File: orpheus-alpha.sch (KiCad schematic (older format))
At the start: 56 parts, among them J1 Signal in, J2 AC in, J3 Signal out, J4 uC, U1 OPA2134, U2 PGA2311, U3 LM317_3PinPackage, U4 LM337_SOT223, U5 LM7805_TO220

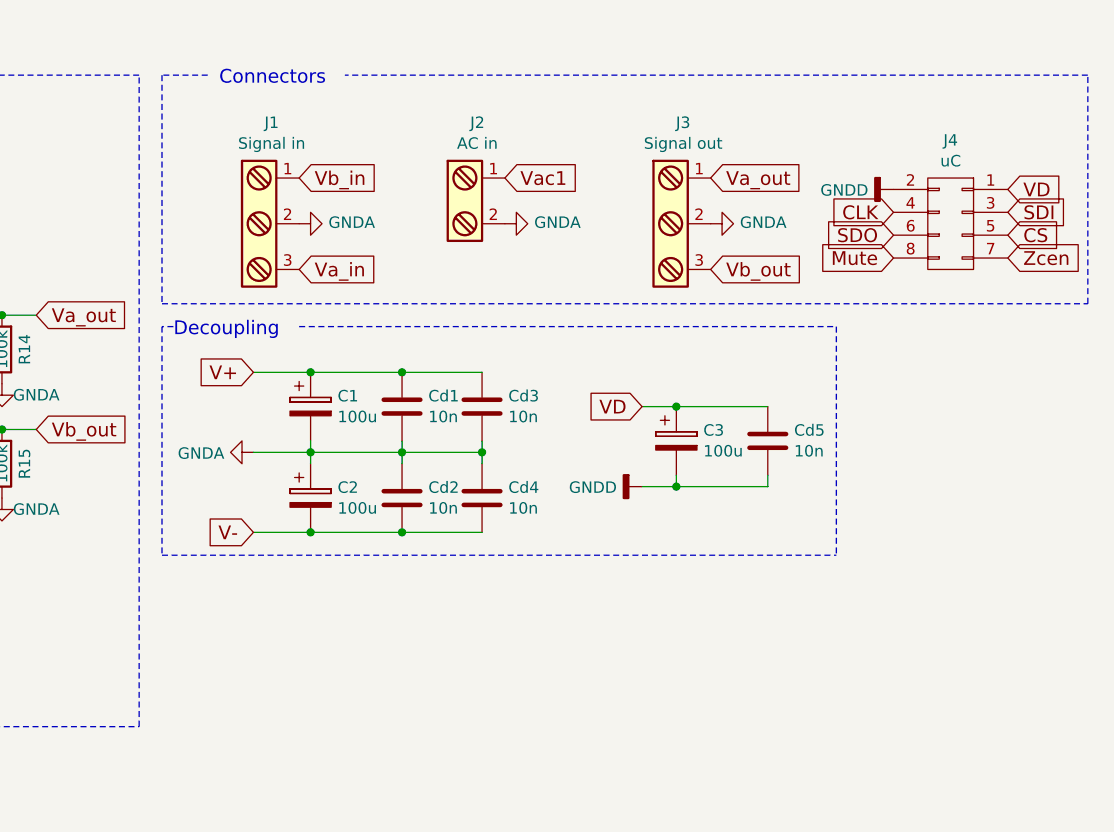
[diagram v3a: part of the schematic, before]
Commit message: Added optional power connectors
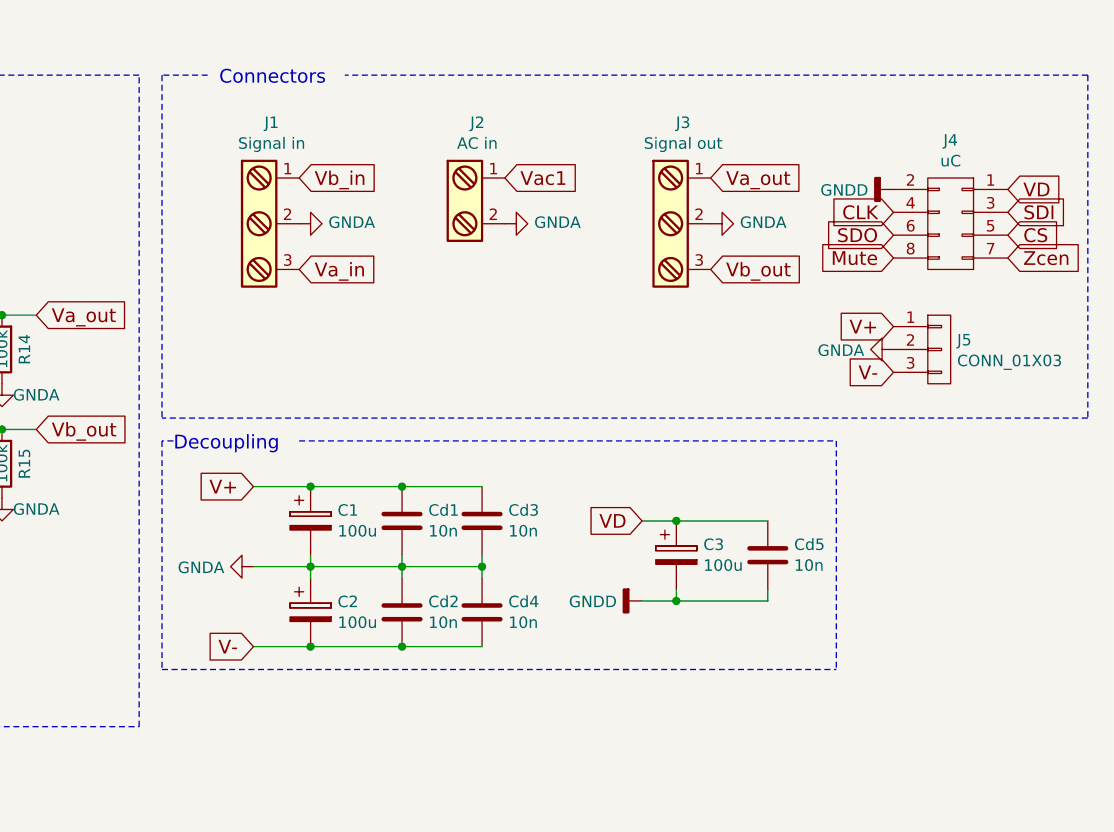
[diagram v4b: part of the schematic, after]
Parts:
- added J5: CONN_01X03, Pin_Headers:Pin_Header_Straight_1x03_Pitch2.54mm, symbol CONN_01X03
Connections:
- net GNDA: now also J5.2 (P2)
- net V+: now also J5.1 (P1)
- net V-: now also J5.3 (P3)
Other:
- moved on the sheet: C1, C2, C3, Cd1, Cd2, Cd3, Cd4, Cd5
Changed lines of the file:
@@
 Text GLabel 2150 1400 3    60   Input ~ 0
 V-
-Text GLabel 7050 1850 0    60   Input ~ 0
+Text GLabel 7050 2350 0    60   Input ~ 0
 V+
-Text GLabel 7050 2550 0    60   Input ~ 0
+Text GLabel 7050 3050 0    60   Input ~ 0
 V-
 $Comp
 L C Cd1
 U 1 1 59B85869
-P 7700 2000
-F 0 "Cd1" H 7815 2046 50  0000 L CNN
-F 1 "10n" H 7815 1955 50  0000 L CNN
-F 2 "Capacitors_SMD:C_0603_HandSoldering" H 7738 1850 50  0001 C CNN
-F 3 "" H 7700 2000 50  0001 C CNN
-F 4 "06035C103JAT2A" H 7700 2000 60  0001 C CNN "manf#"
-	1    7700 2000
+P 7700 2500
+F 0 "Cd1" H 7815 2546 50  0000 L CNN
+F 1 "10n" H 7815 2455 50  0000 L CNN
+F 2 "Capacitors_SMD:C_0603_HandSoldering" H 7738 2350 50  0001 C CNN
+F 3 "" H 7700 2500 50  0001 C CNN
+F 4 "06035C103JAT2A" H 7700 2500 60  0001 C CNN "manf#"
+	1    7700 2500
 	1    0    0    -1
 $EndComp
@@
 L C Cd2
 U 1 1 59B858A9
-P 7700 2400
-F 0 "Cd2" H 7815 2446 50  0000 L CNN
-F 1 "10n" H 7815 2355 50  0000 L CNN
-F 2 "Capacitors_SMD:C_0603_HandSoldering" H 7738 2250 50  0001 C CNN
-F 3 "" H 7700 2400 50  0001 C CNN
-F 4 "06035C103JAT2A" H 7700 2400 60  0001 C CNN "manf#"
-	1    7700 2400
+P 7700 2900
+F 0 "Cd2" H 7815 2946 50  0000 L CNN
+F 1 "10n" H 7815 2855 50  0000 L CNN
+F 2 "Capacitors_SMD:C_0603_HandSoldering" H 7738 2750 50  0001 C CNN
+F 3 "" H 7700 2900 50  0001 C CNN
+F 4 "06035C103JAT2A" H 7700 2900 60  0001 C CNN "manf#"
+	1    7700 2900
 	1    0    0    -1
 $EndComp
@@
 L CP C1
 U 1 1 59B85A85
-P 7300 2000
-F 0 "C1" H 7418 2046 50  0000 L CNN
-F 1 "100u" H 7418 1955 50  0000 L CNN
-F 2 "Capacitors_THT:CP_Radial_D5.0mm_P2.00mm" H 7338 1850 50  0001 C CNN
-F 3 "" H 7300 2000 50  0001 C CNN
-F 4 "UFW1C101MDD1TD" H 7300 2000 60  0001 C CNN "manf#"
-F 5 "16V" H 7300 2000 60  0001 C CNN "Voltage"
-	1    7300 2000
+P 7300 2500
+F 0 "C1" H 7418 2546 50  0000 L CNN
+F 1 "100u" H 7418 2455 50  0000 L CNN
+F 2 "Capacitors_THT:CP_Radial_D5.0mm_P2.00mm" H 7338 2350 50  0001 C CNN
+F 3 "" H 7300 2500 50  0001 C CNN
+F 4 "UFW1C101MDD1TD" H 7300 2500 60  0001 C CNN "manf#"
+F 5 "16V" H 7300 2500 60  0001 C CNN "Voltage"
+	1    7300 2500
 	1    0    0    -1
 $EndComp
@@
 L CP C2
 U 1 1 59B85AD5
-P 7300 2400
-F 0 "C2" H 7418 2446 50  0000 L CNN
-F 1 "100u" H 7418 2355 50  0000 L CNN
-F 2 "Capacitors_THT:CP_Radial_D5.0mm_P2.00mm" H 7338 2250 50  0001 C CNN
-F 3 "" H 7300 2400 50  0001 C CNN
-F 4 "16V" H 7300 2400 60  0001 C CNN "Voltage"
-	1    7300 2400
+P 7300 2900
+F 0 "C2" H 7418 2946 50  0000 L CNN
+F 1 "100u" H 7418 2855 50  0000 L CNN
+F 2 "Capacitors_THT:CP_Radial_D5.0mm_P2.00mm" H 7338 2750 50  0001 C CNN
+F 3 "" H 7300 2900 50  0001 C CNN
+F 4 "16V" H 7300 2900 60  0001 C CNN "Voltage"
+	1    7300 2900
 	1    0    0    -1
 $EndComp
@@
 L C Cd3
 U 1 1 59B85DFC
-P 8050 2000
-F 0 "Cd3" H 8165 2046 50  0000 L CNN
-F 1 "10n" H 8165 1955 50  0000 L CNN
-F 2 "Capacitors_SMD:C_0603_HandSoldering" H 8088 1850 50  0001 C CNN
-F 3 "" H 8050 2000 50  0001 C CNN
-F 4 "06035C103JAT2A" H 8050 2000 60  0001 C CNN "manf#"
-	1    8050 2000
+P 8050 2500
+F 0 "Cd3" H 8165 2546 50  0000 L CNN
+F 1 "10n" H 8165 2455 50  0000 L CNN
+F 2 "Capacitors_SMD:C_0603_HandSoldering" H 8088 2350 50  0001 C CNN
+F 3 "" H 8050 2500 50  0001 C CNN
+F 4 "06035C103JAT2A" H 8050 2500 60  0001 C CNN "manf#"
+	1    8050 2500
 	1    0    0    -1
 $EndComp
@@
 L C Cd4
 U 1 1 59B85E65
-P 8050 2400
-F 0 "Cd4" H 8165 2446 50  0000 L CNN
-F 1 "10n" H 8165 2355 50  0000 L CNN
-F 2 "Capacitors_SMD:C_0603_HandSoldering" H 8088 2250 50  0001 C CNN
-F 3 "" H 8050 2400 50  0001 C CNN
-F 4 "06035C103JAT2A" H 8050 2400 60  0001 C CNN "manf#"
-	1    8050 2400
-	1    0    0    -1
-$EndComp
-Text Notes 6700 1700 0    60   ~ 0
+P 8050 2900
+F 0 "Cd4" H 8165 2946 50  0000 L CNN
+F 1 "10n" H 8165 2855 50  0000 L CNN
+F 2 "Capacitors_SMD:C_0603_HandSoldering" H 8088 2750 50  0001 C CNN
+F 3 "" H 8050 2900 50  0001 C CNN
+F 4 "06035C103JAT2A" H 8050 2900 60  0001 C CNN "manf#"
+	1    8050 2900
+	1    0    0    -1
+$EndComp
+Text Notes 6700 2200 0    60   ~ 0
 Decoupling
 $Comp
@@
 Text Notes 6900 600  0    60   ~ 0
 Connectors
-Text GLabel 8750 2000 0    60   Input ~ 0
+Text GLabel 8750 2500 0    60   Input ~ 0
 VD
 $Comp
 L CP C3
 U 1 1 59B8A02A
-P 8900 2150
-F 0 "C3" H 9018 2196 50  0000 L CNN
-F 1 "100u" H 9018 2105 50  0000 L CNN
-F 2 "Capacitors_THT:CP_Radial_D5.0mm_P2.00mm" H 8938 2000 50  0001 C CNN
-F 3 "" H 8900 2150 50  0001 C CNN
-F 4 "16V" H 8900 2150 60  0001 C CNN "Voltage"
-	1    8900 2150
+P 8900 2650
+F 0 "C3" H 9018 2696 50  0000 L CNN
+F 1 "100u" H 9018 2605 50  0000 L CNN
+F 2 "Capacitors_THT:CP_Radial_D5.0mm_P2.00mm" H 8938 2500 50  0001 C CNN
+F 3 "" H 8900 2650 50  0001 C CNN
+F 4 "16V" H 8900 2650 60  0001 C CNN "Voltage"
+	1    8900 2650
 	1    0    0    -1
 $EndComp
@@
 L C Cd5
 U 1 1 59B8A06F
-P 9300 2150
-F 0 "Cd5" H 9415 2196 50  0000 L CNN
-F 1 "10n" H 9415 2105 50  0000 L CNN
-F 2 "Capacitors_SMD:C_0603_HandSoldering" H 9338 2000 50  0001 C CNN
-F 3 "" H 9300 2150 50  0001 C CNN
-F 4 "06035C103JAT2A" H 9300 2150 60  0001 C CNN "manf#"
-	1    9300 2150
+P 9300 2650
+F 0 "Cd5" H 9415 2696 50  0000 L CNN
+F 1 "10n" H 9415 2605 50  0000 L CNN
+F 2 "Capacitors_SMD:C_0603_HandSoldering" H 9338 2500 50  0001 C CNN
+F 3 "" H 9300 2650 50  0001 C CNN
+F 4 "06035C103JAT2A" H 9300 2650 60  0001 C CNN "manf#"
+	1    9300 2650
 	1    0    0    -1
 $EndComp
@@
 Connection ~ 1100 1000
 Wire Wire Line
-	7050 1850 8050 1850
-Wire Wire Line
-	7050 2550 8050 2550
-Wire Wire Line
-	7050 2200 8050 2200
-Connection ~ 7300 1850
-Wire Wire Line
-	7300 2150 7300 2250
-Connection ~ 7300 2200
-Wire Wire Line
-	8050 2150 8050 2250
-Connection ~ 8050 2200
-Connection ~ 7700 1850
-Wire Wire Line
-	7700 2150 7700 2250
-Connection ~ 7700 2200
-Connection ~ 7300 2550
-Connection ~ 7700 2550
-Wire Notes Line
-	6700 1650 6650 1650
-Wire Notes Line
-	6650 1650 6650 2650
-Wire Notes Line
-	6650 2650 9600 2650
-Wire Notes Line
-	7250 1650 9600 1650
+	7050 2350 8050 2350
+Wire Wire Line
+	7050 3050 8050 3050
+Wire Wire Line
+	7050 2700 8050 2700
+Connection ~ 7300 2350
+Wire Wire Line
+	7300 2650 7300 2750
+Connection ~ 7300 2700
+Wire Wire Line
+	8050 2650 8050 2750
+Connection ~ 8050 2700
+Connection ~ 7700 2350
+Wire Wire Line
+	7700 2650 7700 2750
+Connection ~ 7700 2700
+Connection ~ 7300 3050
+Connection ~ 7700 3050
+Wire Notes Line
+	6700 2150 6650 2150
+Wire Notes Line
+	6650 2150 6650 3150
+Wire Notes Line
+	6650 3150 9600 3150
+Wire Notes Line
+	7250 2150 9600 2150
 Wire Wire Line
 	1500 3750 2000 3750
@@
 	6850 550  6650 550
 Wire Notes Line
-	6650 550  6650 1550
-Wire Notes Line
-	6650 1550 10700 1550
-Wire Notes Line
-	10700 1550 10700 550
+	6650 550  6650 2050
+Wire Notes Line
+	10700 550  10700 2050
 Wire Notes Line
 	10700 550  7450 550
 Wire Wire Line
-	8750 2000 9300 2000
-Wire Wire Line
-	9300 2350 9300 2300
-Wire Wire Line
-	8750 2350 9300 2350
-Wire Wire Line
-	8900 2300 8900 2350
-Connection ~ 8900 2350
-Connection ~ 8900 2000
-Wire Notes Line
-	9600 1650 9600 2650
+	8750 2500 9300 2500
+Wire Wire Line
+	9300 2850 9300 2800
+Wire Wire Line
+	8750 2850 9300 2850
+Wire Wire Line
+	8900 2800 8900 2850
+Connection ~ 8900 2850
+Connection ~ 8900 2500
+Wire Notes Line
+	9600 2150 9600 3150
 Wire Wire Line
 	900  6350 900  5850
@@
 L GNDA #PWR09
 U 1 1 59BC7B64
-P 7050 2200
-F 0 "#PWR09" H 7050 1950 50  0001 C CNN
-F 1 "GNDA" V 7055 2073 50  0000 R CNN
-F 2 "" H 7050 2200 50  0001 C CNN
-F 3 "" H 7050 2200 50  0001 C CNN
-	1    7050 2200
+P 7050 2700
+F 0 "#PWR09" H 7050 2450 50  0001 C CNN
+F 1 "GNDA" V 7055 2573 50  0000 R CNN
+F 2 "" H 7050 2700 50  0001 C CNN
+F 3 "" H 7050 2700 50  0001 C CNN
+	1    7050 2700
 	0    1    1    0
 $EndComp
@@
 L GNDD #PWR011
 U 1 1 59BC7D4A
-P 8750 2350
-F 0 "#PWR011" H 8750 2100 50  0001 C CNN
-F 1 "GNDD" V 8754 2240 50  0000 R CNN
-F 2 "" H 8750 2350 50  0001 C CNN
-F 3 "" H 8750 2350 50  0001 C CNN
-	1    8750 2350
+P 8750 2850
+F 0 "#PWR011" H 8750 2600 50  0001 C CNN
+F 1 "GNDD" V 8754 2740 50  0000 R CNN
+F 2 "" H 8750 2850 50  0001 C CNN
+F 3 "" H 8750 2850 50  0001 C CNN
+	1    8750 2850
 	0    1    1    0
 $EndComp
@@
 	8650 5250 8650 5700
 Connection ~ 8650 5700
+$Comp
+L CONN_01X03 J5
+U 1 1 59E385EB
+P 10050 1750
+F 0 "J5" H 10128 1791 50  0000 L CNN
+F 1 "CONN_01X03" H 10128 1700 50  0000 L CNN
+F 2 "Pin_Headers:Pin_Header_Straight_1x03_Pitch2.54mm" H 10050 1750 50  0001 C CNN
+F 3 "" H 10050 1750 50  0001 C CNN
+	1    10050 1750
+	1    0    0    -1
+$EndComp
+$Comp
+L GNDA #PWR019
+U 1 1 59E38737
+P 9850 1750
+F 0 "#PWR019" H 9850 1500 50  0001 C CNN
+F 1 "GNDA" V 9855 1622 50  0000 R CNN
+F 2 "" H 9850 1750 50  0001 C CNN
+F 3 "" H 9850 1750 50  0001 C CNN
+	1    9850 1750
+	0    1    1    0
+$EndComp
+Text GLabel 9850 1650 0    60   Input ~ 0
+V+
+Text GLabel 9850 1850 0    60   Input ~ 0
+V-
+Wire Notes Line
+	10700 2050 6650 2050
 $EndSCHEMATC

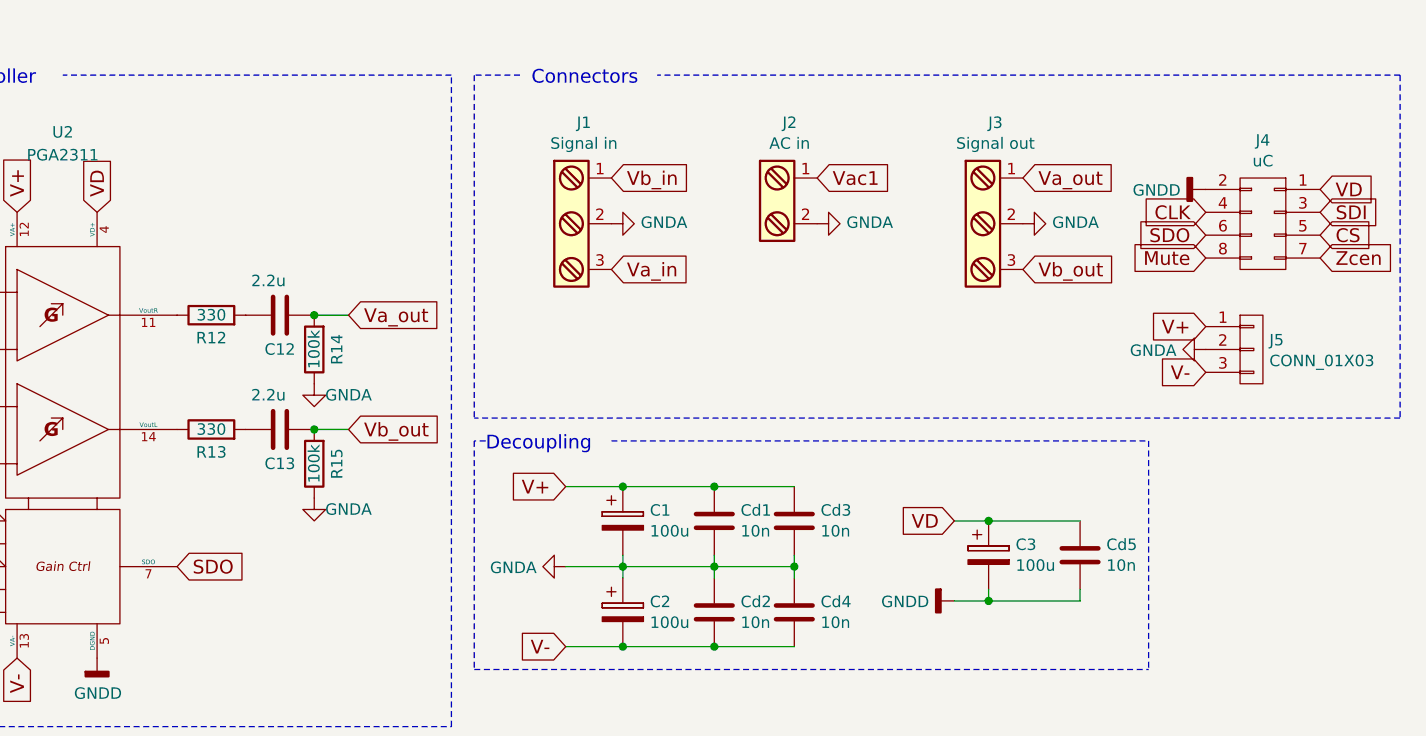
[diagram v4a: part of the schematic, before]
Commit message: New layout, "debug" connection pads at the edge
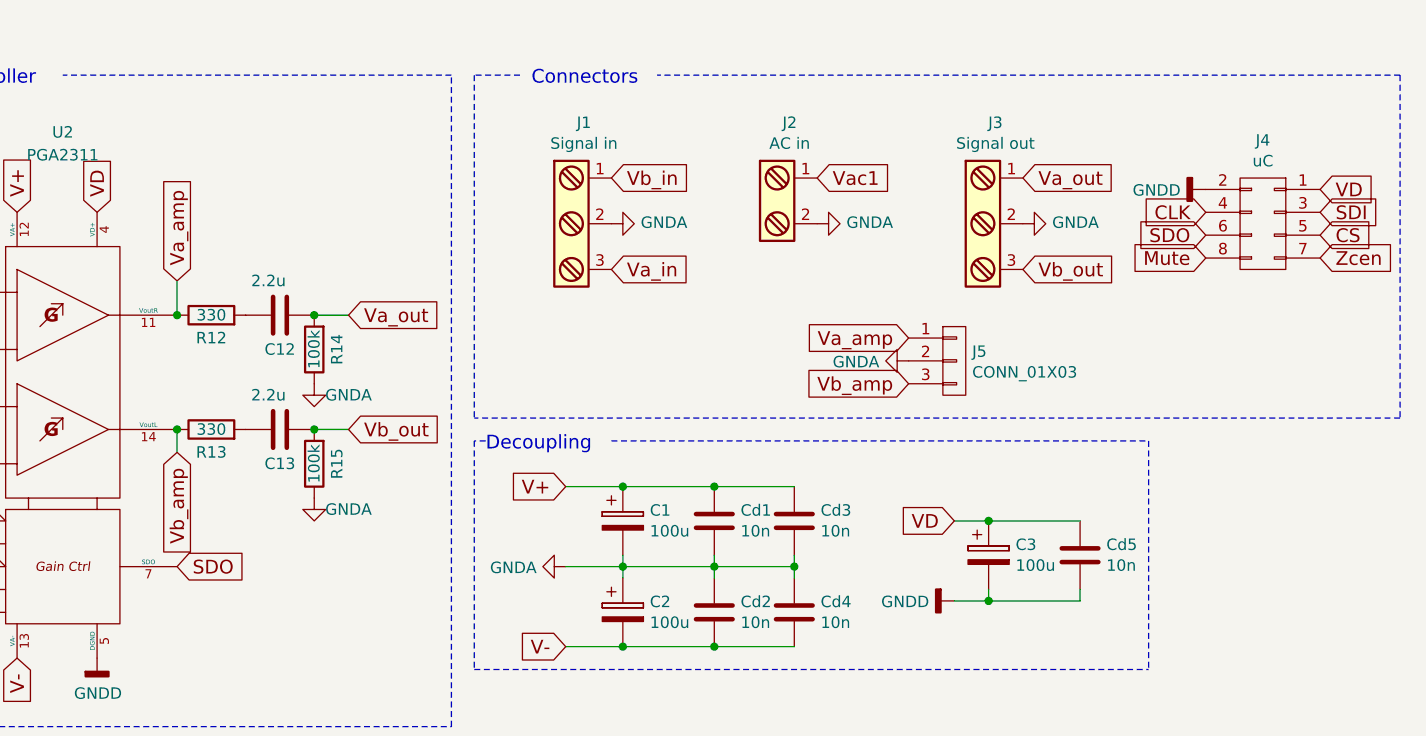
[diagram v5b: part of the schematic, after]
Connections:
- net V+: no longer J5.1 (P1)
- net V-: no longer J5.3 (P3)
- net Va_amp: now reaches R12.1, U2.11 (VoutR)
- net Va_amp: now also J5.1 (P1)
- net Vb_amp: now reaches R13.1, U2.14 (VoutL)
- net Vb_amp: now also J5.3 (P3)

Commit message: Added heatsinks
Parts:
- U5: footprint TO_SOT_Packages_THT:TO-220_Vertical -> orpheus-alpha:TO-220_Vertical
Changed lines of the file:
@@
 F 0 "U5" H 8050 5192 50  0000 C CNN
 F 1 "LM7805_TO220" H 8050 5101 50  0000 C CNN
-F 2 "TO_SOT_Packages_THT:TO-220_Vertical" H 8050 5175 50  0001 C CIN
+F 2 "orpheus-alpha:TO-220_Vertical" H 8050 5175 50  0001 C CIN
 F 3 "http://www.mouser.com/ds/2/308/LM7805-1124977.pdf" H 8050 4900 50  0001 C CNN
 F 4 "LM7805CT" H 8050 4950 60  0001 C CNN "manf#"

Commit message: Changed footprint of PSU capacitors
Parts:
- C14, C4, C5, C6, C7: footprint Capacitors_THT:CP_Radial_D10.0mm_P7.50mm -> Capacitors_THT:CP_Radial_D10.0mm_P5.00mm
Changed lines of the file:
@@
 F 0 "C6" H 2218 5696 50  0000 L CNN
 F 1 "1m" H 2218 5605 50  0000 L CNN
-F 2 "Capacitors_THT:CP_Radial_D10.0mm_P7.50mm" H 2138 5500 50  0001 C CNN
+F 2 "Capacitors_THT:CP_Radial_D10.0mm_P5.00mm" H 2138 5500 50  0001 C CNN
 F 3 "" H 2100 5650 50  0001 C CNN
 F 4 "25V" H 1350 5650 60  0001 C CNN "Voltage"
@@
 F 0 "C7" H 2218 6596 50  0000 L CNN
 F 1 "1m" H 2218 6505 50  0000 L CNN
-F 2 "Capacitors_THT:CP_Radial_D10.0mm_P7.50mm" H 2138 6400 50  0001 C CNN
+F 2 "Capacitors_THT:CP_Radial_D10.0mm_P5.00mm" H 2138 6400 50  0001 C CNN
 F 3 "" H 2100 6550 50  0001 C CNN
 F 4 "25V" H 1350 5650 60  0001 C CNN "Voltage"
@@
 F 0 "C4" H 1468 5696 50  0000 L CNN
 F 1 "1m" H 1468 5605 50  0000 L CNN
-F 2 "Capacitors_THT:CP_Radial_D10.0mm_P7.50mm" H 1388 5500 50  0001 C CNN
+F 2 "Capacitors_THT:CP_Radial_D10.0mm_P5.00mm" H 1388 5500 50  0001 C CNN
 F 3 "" H 1350 5650 50  0001 C CNN
 F 4 "25V" H 1350 5650 60  0001 C CNN "Voltage"
@@
 F 0 "C5" H 1468 6596 50  0000 L CNN
 F 1 "1m" H 1468 6505 50  0000 L CNN
-F 2 "Capacitors_THT:CP_Radial_D10.0mm_P7.50mm" H 1388 6400 50  0001 C CNN
+F 2 "Capacitors_THT:CP_Radial_D10.0mm_P5.00mm" H 1388 6400 50  0001 C CNN
 F 3 "" H 1350 6550 50  0001 C CNN
 F 4 "25V" H 1350 5650 60  0001 C CNN "Voltage"
@@
 F 0 "C14" H 7068 5146 50  0000 L CNN
 F 1 "470u" H 7068 5055 50  0000 L CNN
-F 2 "Capacitors_THT:CP_Radial_D10.0mm_P7.50mm" H 6988 4950 50  0001 C CNN
+F 2 "Capacitors_THT:CP_Radial_D10.0mm_P5.00mm" H 6988 4950 50  0001 C CNN
 F 3 "" H 6950 5100 50  0001 C CNN
 F 4 "UFW1E471MPD1TD" H 6950 5100 60  0001 C CNN "manf#"
